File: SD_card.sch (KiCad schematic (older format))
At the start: 5 parts

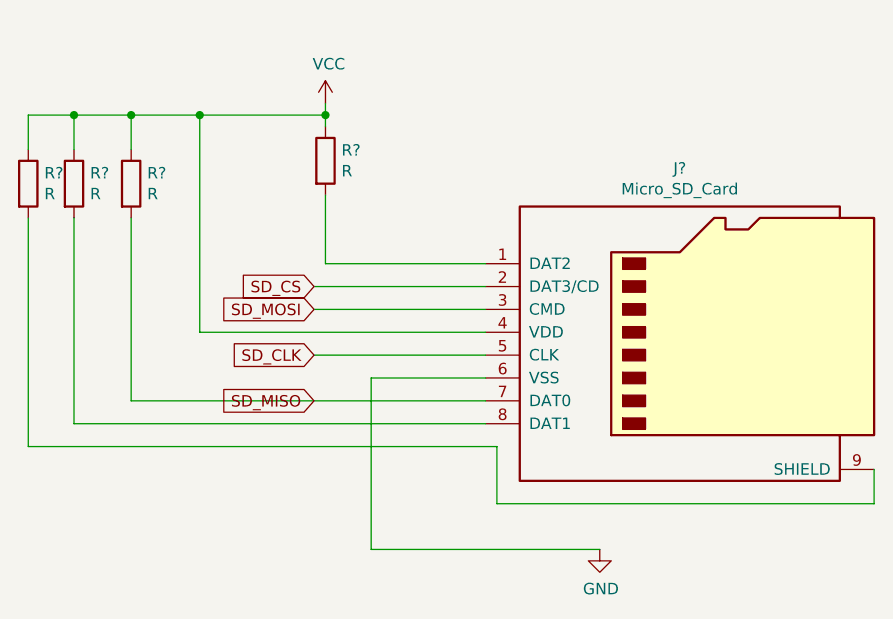
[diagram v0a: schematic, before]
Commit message: 4 layer add
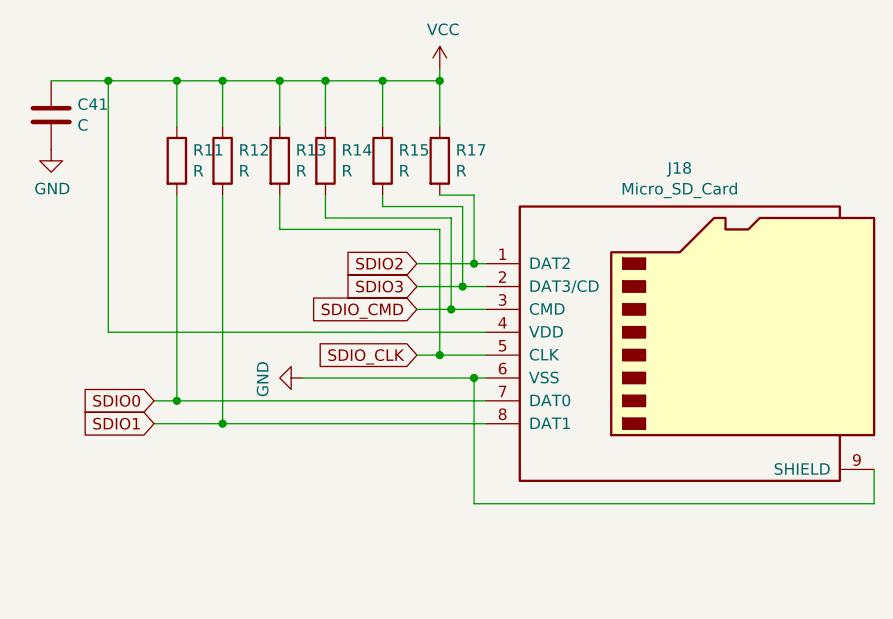
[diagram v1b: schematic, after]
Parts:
- added C41: C, Capacitor_SMD:C_0603_1608Metric, symbol Device:C
- added R11, R12: R, Resistor_SMD:R_0402_1005Metric, symbol Device:R
- J18: renamed from J?; footprint drone_v3:SD_card_mua_duoc -> Pixracer_clone:SUNTECH_ST-TF-003A
- gave numbers to parts that had none: 4
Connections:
- net SD_CLK is gone; now on net SDIO_CLK: J18.5 (CLK)
- net GND: now also J18.9 (SHIELD), C41.2
- net VCC: now also C41.1, R11.1, R12.1
- net SDIO_CLK: now reaches R13.2
- net SDIO_CLK: no longer J18.9 (SHIELD)
- net SDIO1: now reaches J18.8 (DAT1)
- net SDIO1: now also R12.2; no longer R14.2
- net SDIO2: now reaches J18.1 (DAT2), R17.2
- net SD_CS renamed SDIO3
- net SDIO3: now also R15.2
- net SD_MISO renamed SDIO0
- net SDIO0: now also R11.2; no longer R15.2
- net SD_MOSI renamed SDIO_CMD
- net SDIO_CMD: now also R14.2
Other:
- moved on the sheet: R13, R14, R15, R17
